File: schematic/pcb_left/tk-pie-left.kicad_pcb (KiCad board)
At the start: 2 copper layers, 129 x 77.5 mm, 26 parts, among them J1 UART, J2 DBG

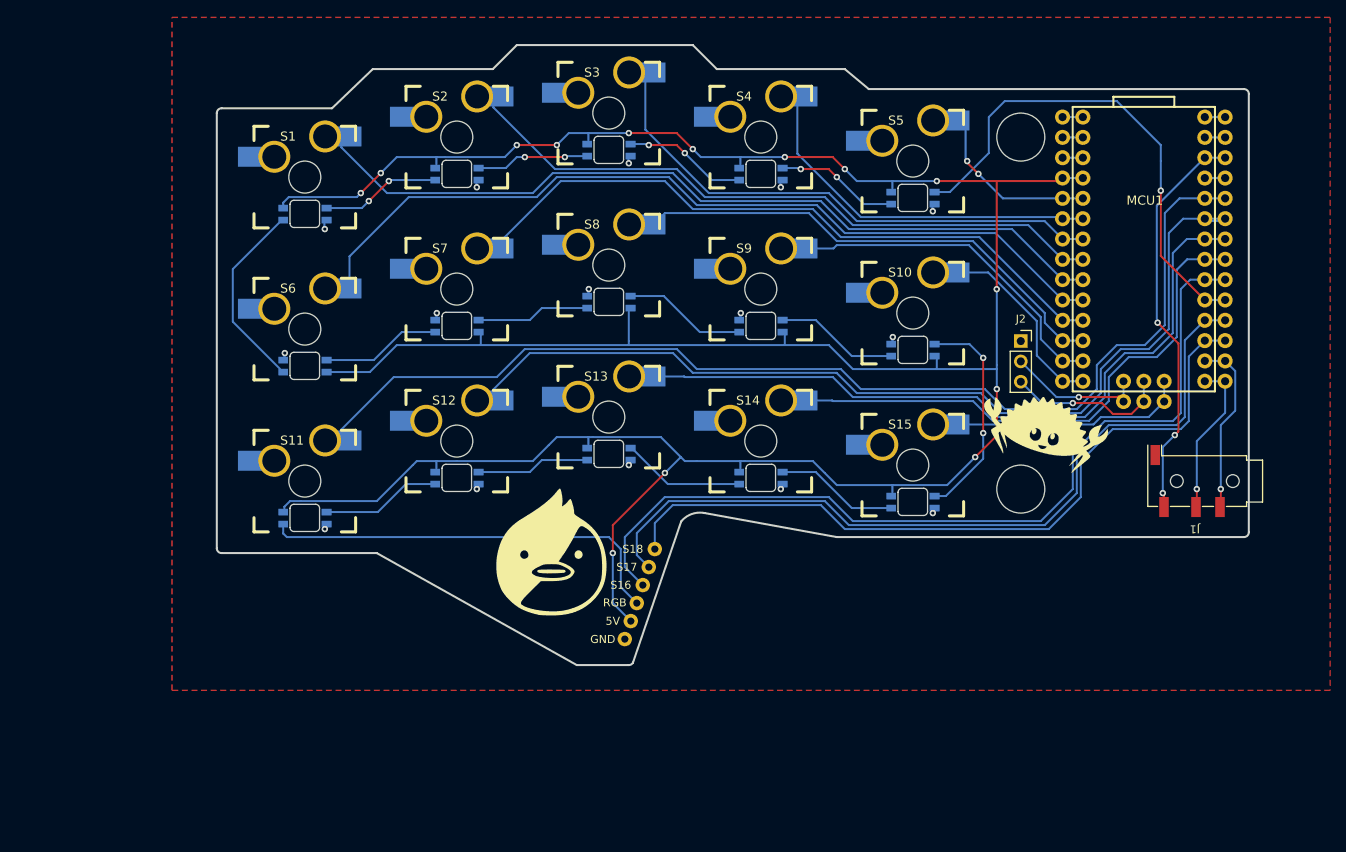
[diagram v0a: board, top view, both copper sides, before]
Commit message: Start wiring up components
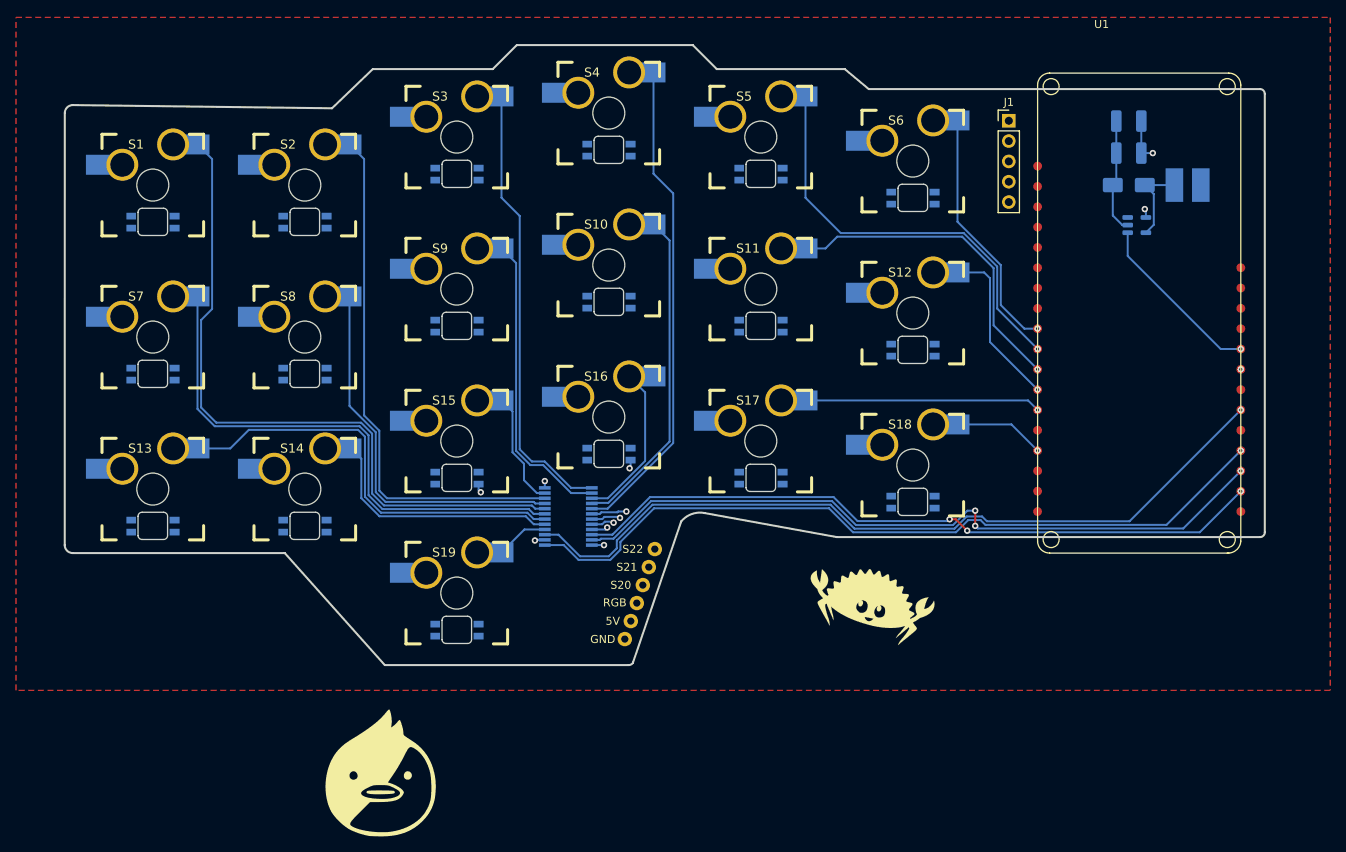
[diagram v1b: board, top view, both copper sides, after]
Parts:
- removed J2: DBG, Connector_PinSocket_2.54mm:PinSocket_1x03_P2.54mm_Vertical
- removed MCU1: ITSYBITSY RP2040, Footprints:ITSYBITSY BREAKOUT
- removed REF** (x2): MountingHole_6mm, MountingHole:MountingHole_6mm
- added C4: 12µF, Capacitor_SMD:C_1210_3225Metric_Pad1.33x2.70mm_HandSolder, B.Cu at (139.0, 35.0)
- added C5: 12µF, Capacitor_SMD:C_1210_3225Metric_Pad1.33x2.70mm_HandSolder, B.Cu at (139.0, 31.0)
- added D1: SS14, Diode_SMD:D_SMA, B.Cu at (139.0, 39.0)
- added IC1: PCA9539PW,118, Footprints:SOP65P640X110-24N, B.Cu at (68.9, 80.4)
- added L2: 22µH, Inductor_SMD:L_Cenker_CKCS5040, B.Cu at (146.3, 39.0)
- added PS1: ME2108C50M5G, Package_TO_SOT_SMD:SOT-23-5, B.Cu at (140.0, 44.0)
- added S1: MX_SW_SOCKET_LED, Footprints:MX_SW_SOCKET_LED, F.Cu at (17.0, 39.0)
- added S13: MX_SW_SOCKET_LED, Footprints:MX_SW_SOCKET_LED, F.Cu at (17.0, 77.0)
- added S19: MX_SW_SOCKET_RGB_REV, Footprints:MX_SW_SOCKET_LED_REV, F.Cu at (55.0, 90.0)
- added S7: MX_SW_SOCKET_RGB_REV, Footprints:MX_SW_SOCKET_LED_REV, F.Cu at (17.0, 58.0)
- added U1: ~, Footprints:DFR1075, F.Cu at (127.6, 25.0)
- J1: value UART -> NiceView Header; footprint Connector_Audio:Jack_3.5mm_KoreanHropartsElec_PJ-320D-4A_Horizontal -> Connector_PinHeader_2.54mm:PinHeader_1x05_P2.54mm_Vertical
- moved J1 50.7 mm to (124.0, 31.0), turned to 0 degrees
- moved S14 1.00 mm to (36.0, 77.0)
- moved S2 1.00 mm to (36.0, 39.0)
- moved S8 1.00 mm to (36.0, 58.0)
- renumbered S8 to S10, S9 to S11, S10 to S12, S11 to S14, S12 to S15, S13 to S16, S14 to S17, S15 to S18, S1 to S2, S2 to S3, S3 to S4, S4 to S5, S5 to S6, S6 to S8, S7 to S9
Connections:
- E4 pad 1: /S16 -> /S20
- E5 pad 1: /S17 -> /S21
- E6 pad 1: /S18 -> /S22
- S10 pad 2: /S8 -> /S10
- S11 pad 2: /S9 -> /S11
- S12 pad 2: /S10 -> /S12
- S14 pad 2: /S11 -> /S14
- S14 pad 6: Net-(E3-Pin_1) -> Net-(S13-DIN)
- S15 pad 2: /S12 -> /S15
- S16 pad 2: /S13 -> /S16
- S17 pad 2: /S14 -> /S17
- S18 pad 2: /S15 -> /S18
- S2 pad 2: /S1 -> /S2
- S2 pad 6: Net-(S1-DOUT) -> Net-(S1-DIN)
- S3 pad 2: /S2 -> /S3
- S4 pad 2: /S3 -> /S4
- S5 pad 2: /S4 -> /S5
- S6 pad 2: /S5 -> /S6
- S8 pad 2: /S6 -> /S8
- S8 pad 5: Net-(S1-DOUT) -> Net-(S7-DOUT)
- S9 pad 2: /S7 -> /S9
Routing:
- net +5V: track 369.8 -> 15.9 mm, vias 14 -> 1
- net /S11: track 140.0 -> 40.7 mm, vias 0 -> 1
- net /GPIOE_RST: track 0.00 -> 99.2 mm, vias 0 -> 1
- net /S12: track 119.2 -> 20.7 mm, vias 0 -> 1
- net /GPIOE_INT: track 0.00 -> 97.0 mm, vias 0 -> 1
- net /GPIOE_SDA: track 0.00 -> 90.1 mm, vias 0 -> 3
- net /S16: track 109.5 -> 20.0 mm
- net /GPIOE_SCL: track 0.00 -> 87.2 mm, vias 0 -> 3
- net /S18: track 93.8 -> 11.4 mm, vias 0 -> 1
- net /S6: track 106.1 -> 31.1 mm, vias 0 -> 1
- net /S17: track 100.2 -> 29.5 mm, vias 0 -> 1
- net /NEOPIXEL_DIN: track 62.4 -> 0.00 mm, vias 1 -> 0
- net Net-(E3-Pin_1): track 51.8 -> 0.00 mm
- net /VBUS: track 50.7 -> 0.00 mm, vias 3 -> 0
- net /S14: track 67.6 -> 31.2 mm
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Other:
- board size 129 x 77.5 mm -> 150 x 77.5 mm
- board text added: "S20"
- board text added: "S21"
- board text added: "S22"
- board text removed: "S16"
- board text removed: "S17"
- board text removed: "S18"

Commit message: Add logic level shifter to schematic
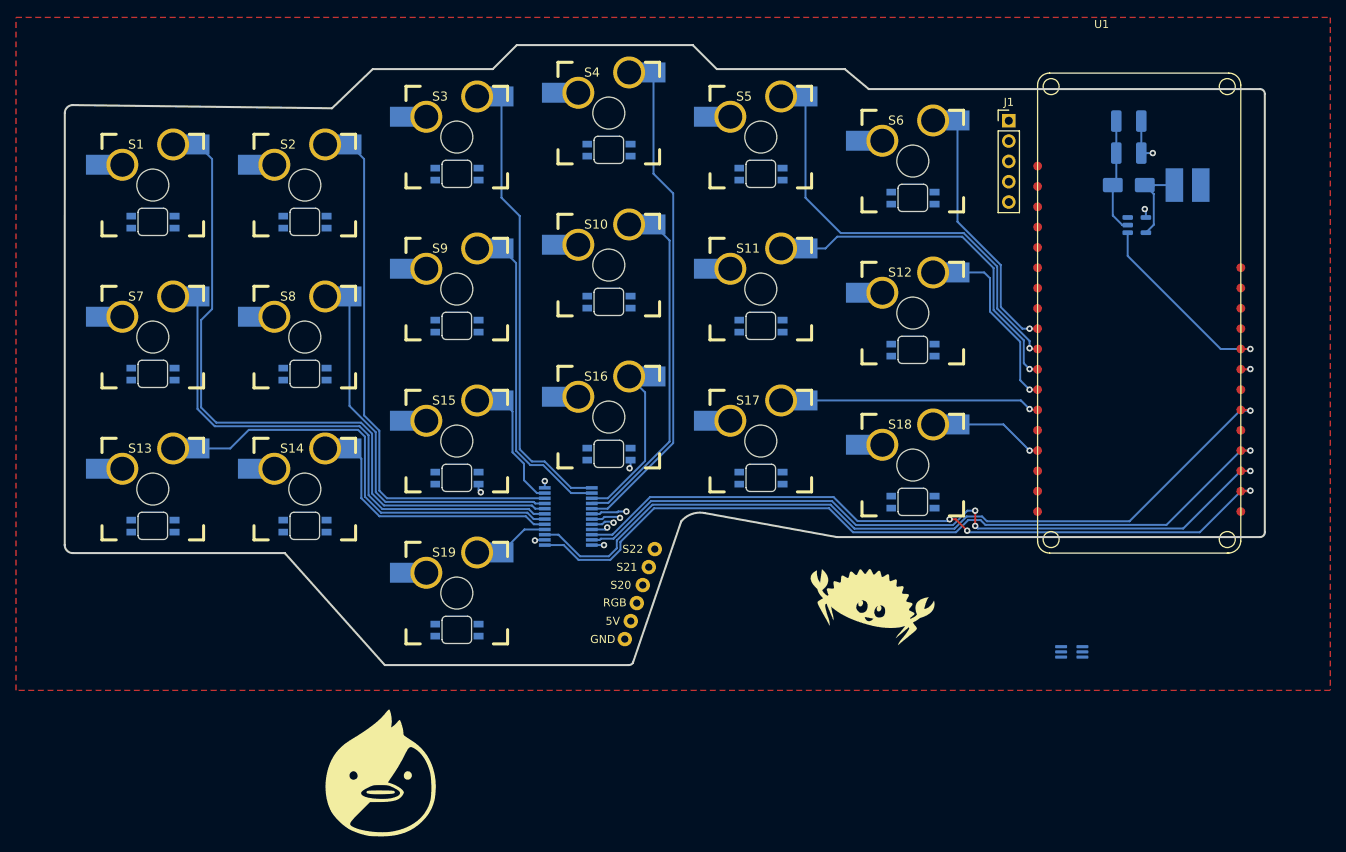
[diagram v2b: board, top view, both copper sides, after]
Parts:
- added U3: SN74LVC1T45DCK, Package_TO_SOT_SMD:SOT-363_SC-70-6_Handsoldering, B.Cu at (131.9, 97.3)
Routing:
- net /GPIOE_SCL: track 87.2 -> 89.7 mm
- net /GPIOE_RST: track 99.2 -> 101.6 mm
- net /GPIOE_SDA: track 90.1 -> 92.5 mm
- net /GPIOE_INT: track 97.0 -> 99.4 mm
- net /5V_EN: track 21.9 -> 24.3 mm
- net /LED_CTRL: track 0.00 -> 1.21 mm
- net /S12: track 20.7 -> 21.3 mm
- net /S11: track 40.7 -> 41.2 mm
- net /S5: track 52.6 -> 53.1 mm

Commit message: Connect ground on left PCB
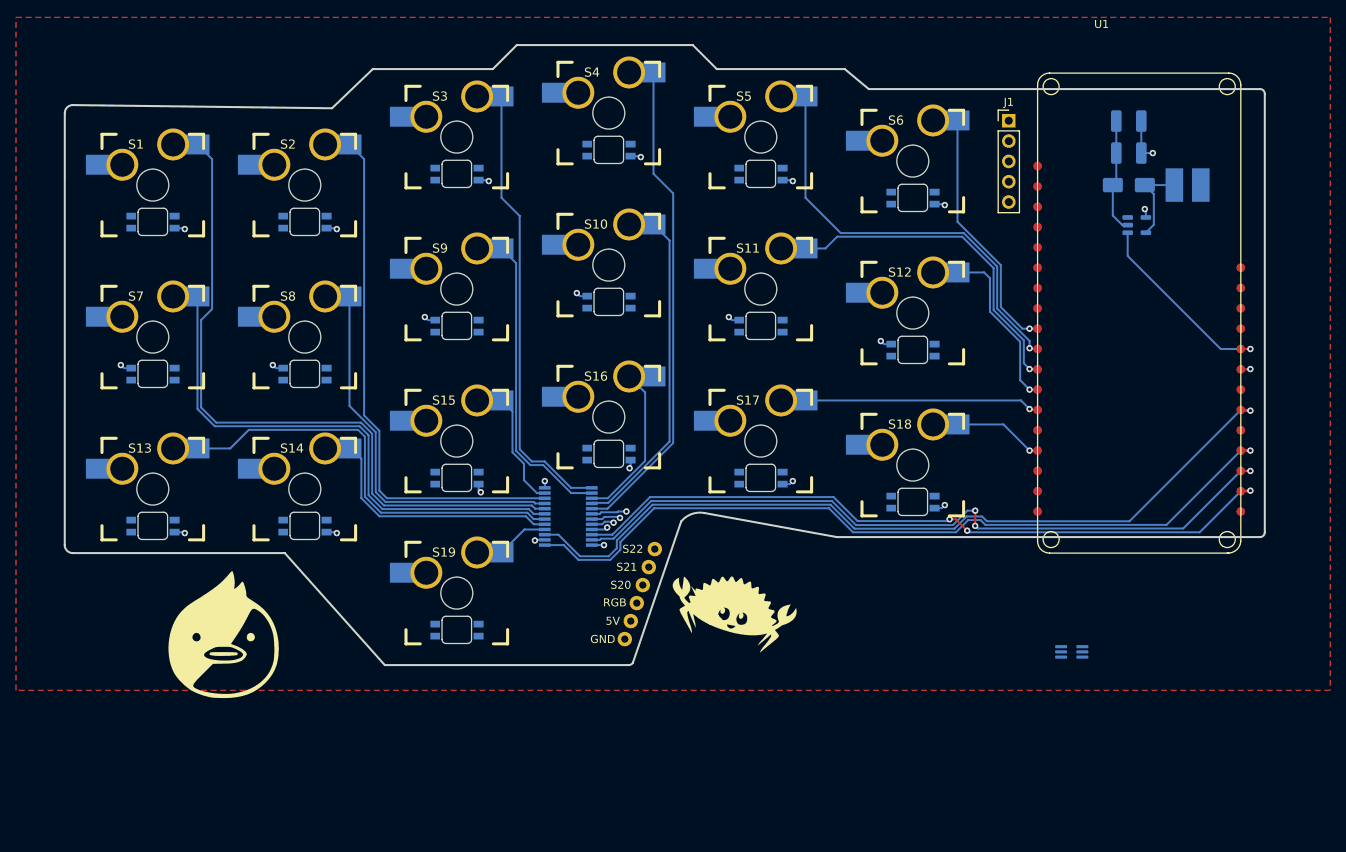
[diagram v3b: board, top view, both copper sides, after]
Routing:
- net GND: track 12.9 -> 35.1 mm, vias 7 -> 23

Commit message: Connect neopixels on left pcb
Also connect missed ground
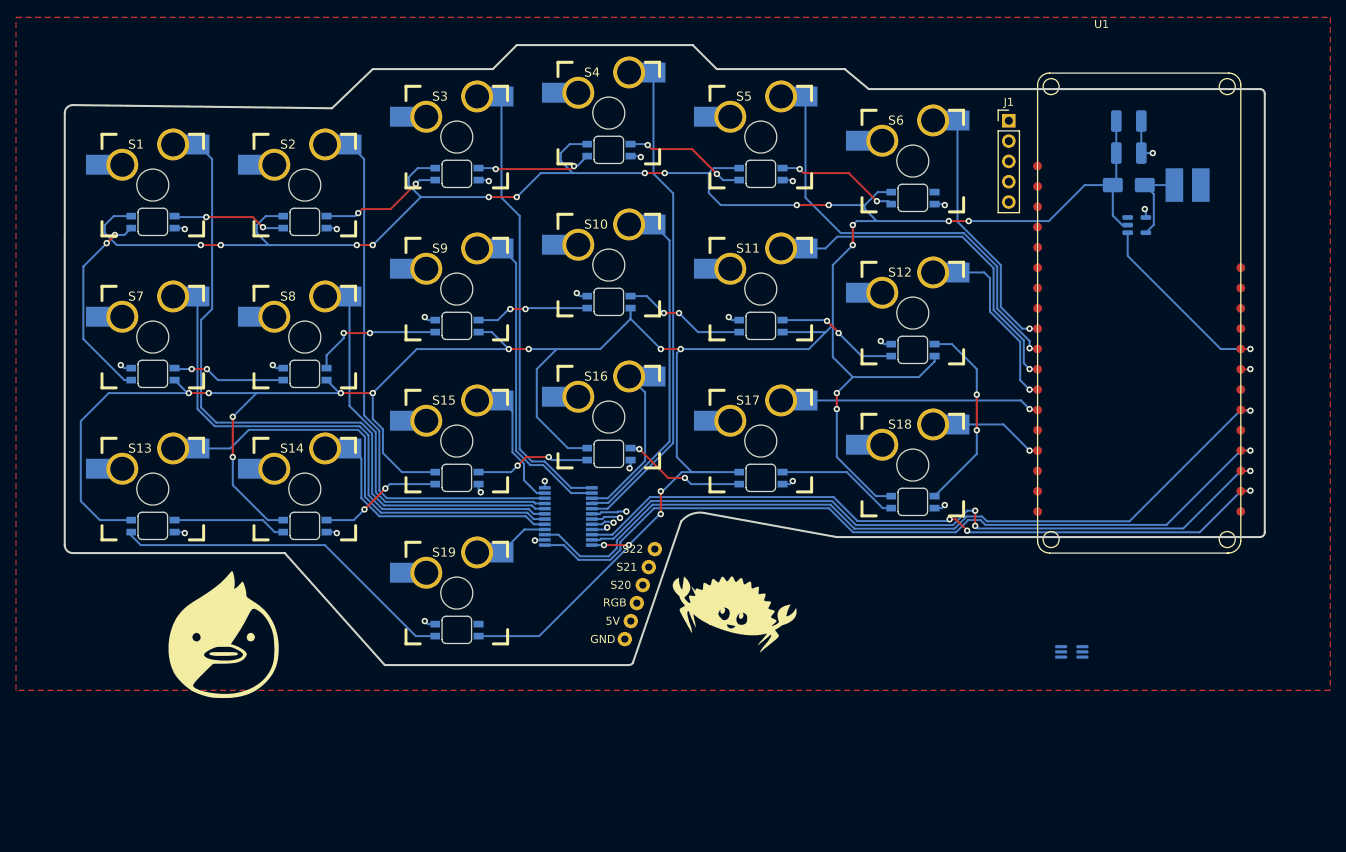
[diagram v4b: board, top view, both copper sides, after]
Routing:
- net +5V: track 15.9 -> 498.2 mm, vias 1 -> 30
- net Net-(S13-DOUT): track 0.00 -> 43.6 mm
- net Net-(S1-DOUT): track 0.00 -> 25.1 mm, vias 0 -> 2
- net Net-(S12-DOUT): track 0.00 -> 24.6 mm, vias 0 -> 2
- net Net-(S8-DOUT): track 0.00 -> 16.8 mm, vias 0 -> 2
- net Net-(S11-DOUT): track 0.00 -> 15.5 mm, vias 0 -> 2
- net Net-(S2-DIN): track 0.00 -> 15.4 mm, vias 0 -> 2
- net Net-(S14-DIN): track 0.00 -> 15.4 mm, vias 0 -> 2
- net Net-(S17-DIN): track 0.00 -> 15.4 mm
- net Net-(S5-DIN): track 0.00 -> 15.4 mm, vias 0 -> 2
- net Net-(S10-DOUT): track 0.00 -> 15.4 mm, vias 0 -> 2
- net Net-(S4-DIN): track 0.00 -> 15.4 mm, vias 0 -> 2
- net Net-(S16-DIN): track 0.00 -> 15.4 mm, vias 0 -> 2
- net Net-(S15-DIN): track 0.00 -> 14.5 mm, vias 0 -> 2
- net Net-(S3-DIN): track 0.00 -> 14.3 mm, vias 0 -> 2
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
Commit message: Move and connect logic level thingy
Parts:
- moved U3 37.4 mm to (122.5, 61.1), turned to -90 degrees
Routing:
- net /LED_CTRL: track 1.21 -> 34.8 mm
- net +3.3V: track 0.00 -> 28.6 mm, vias 0 -> 5
- net /NEOPIXEL_DIN: track 0.00 -> 25.4 mm, vias 0 -> 2
- net +5V: track 498.2 -> 505.6 mm, vias 30 -> 32
- net GND: track 36.6 -> 39.9 mm, vias 24 -> 26
